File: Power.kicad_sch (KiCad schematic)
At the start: 0 parts

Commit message: Updated power and MCU schem
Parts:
- added C10: 1uF, PCM_JLCPCB:C_0603, symbol PCM_JLCPCB-Capacitors:0603,1uF
- added C11: 2.2uF, PCM_JLCPCB:C_0603, symbol PCM_JLCPCB-Capacitors:0603,2.2uF
- added J1: Conn_01x02, symbol Connector_Generic:Conn_01x02
- added SW1: SW_Push, symbol Switch:SW_Push
- added U6: NPM1300-QEAA-R7, QFN32_5X5_NOR, symbol 2026-04-08_23-52-45:NPM1300-QEAA-R7
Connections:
- new net +BATT: C11.1, U6.19 (VBAT)
- new net GND: C10.2, C11.2, SW1.1, U6.18 (NTC)
- new net NPM_INT: U6.8 (GPIO1)
- new net RESET: SW1.2, U6.7 (GPIO0)
- new net VBUS: C10.1, U6.21 (VBUS)

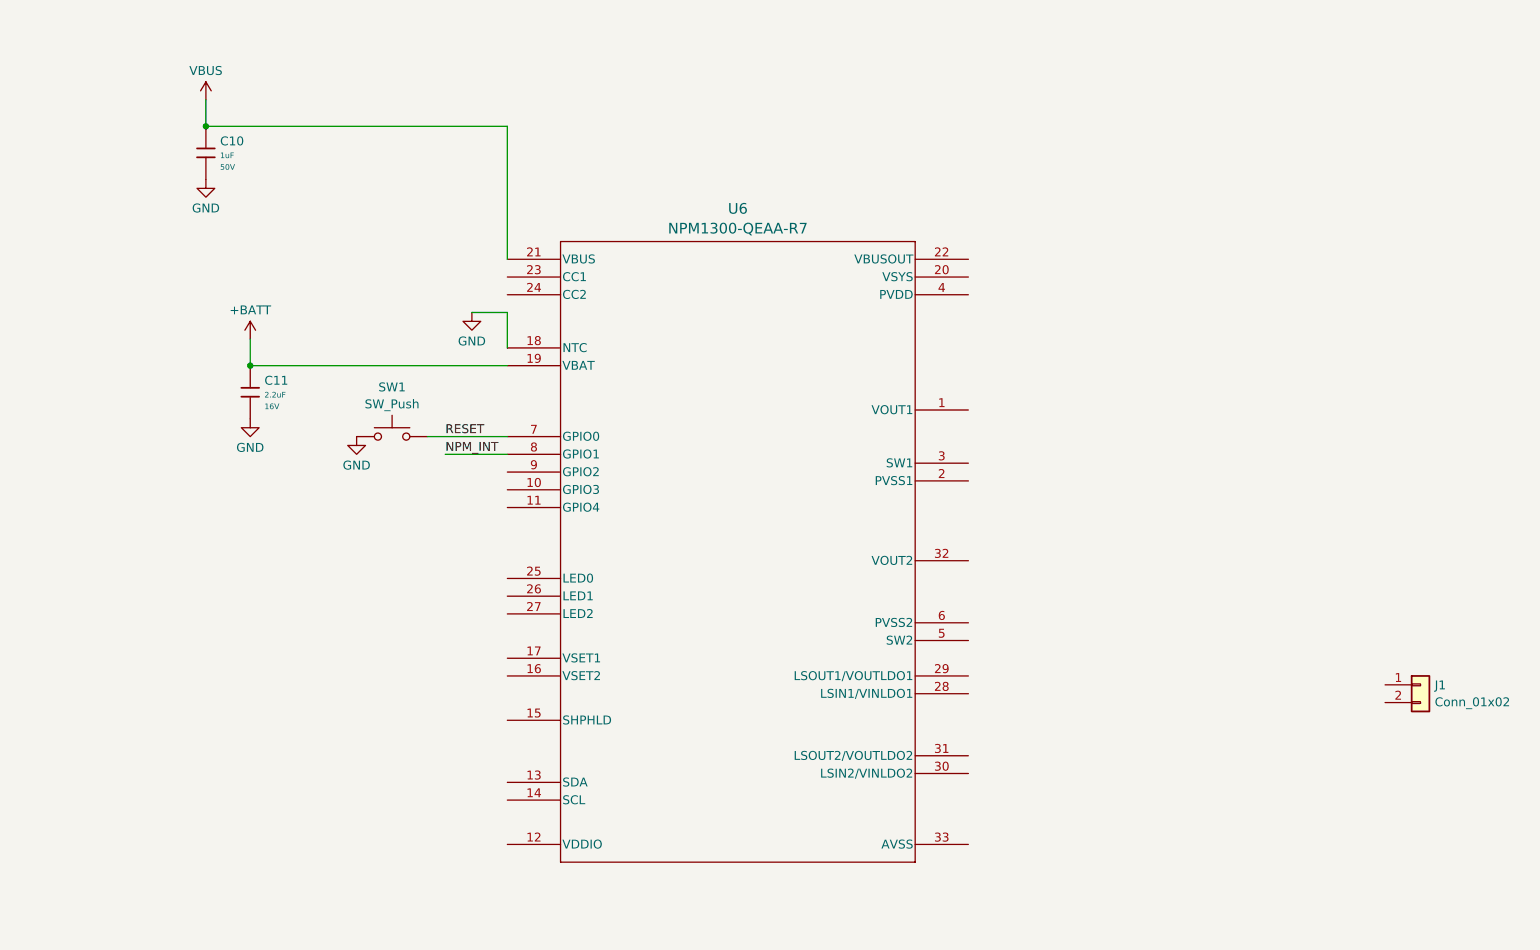
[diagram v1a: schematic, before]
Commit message: PMIC integration
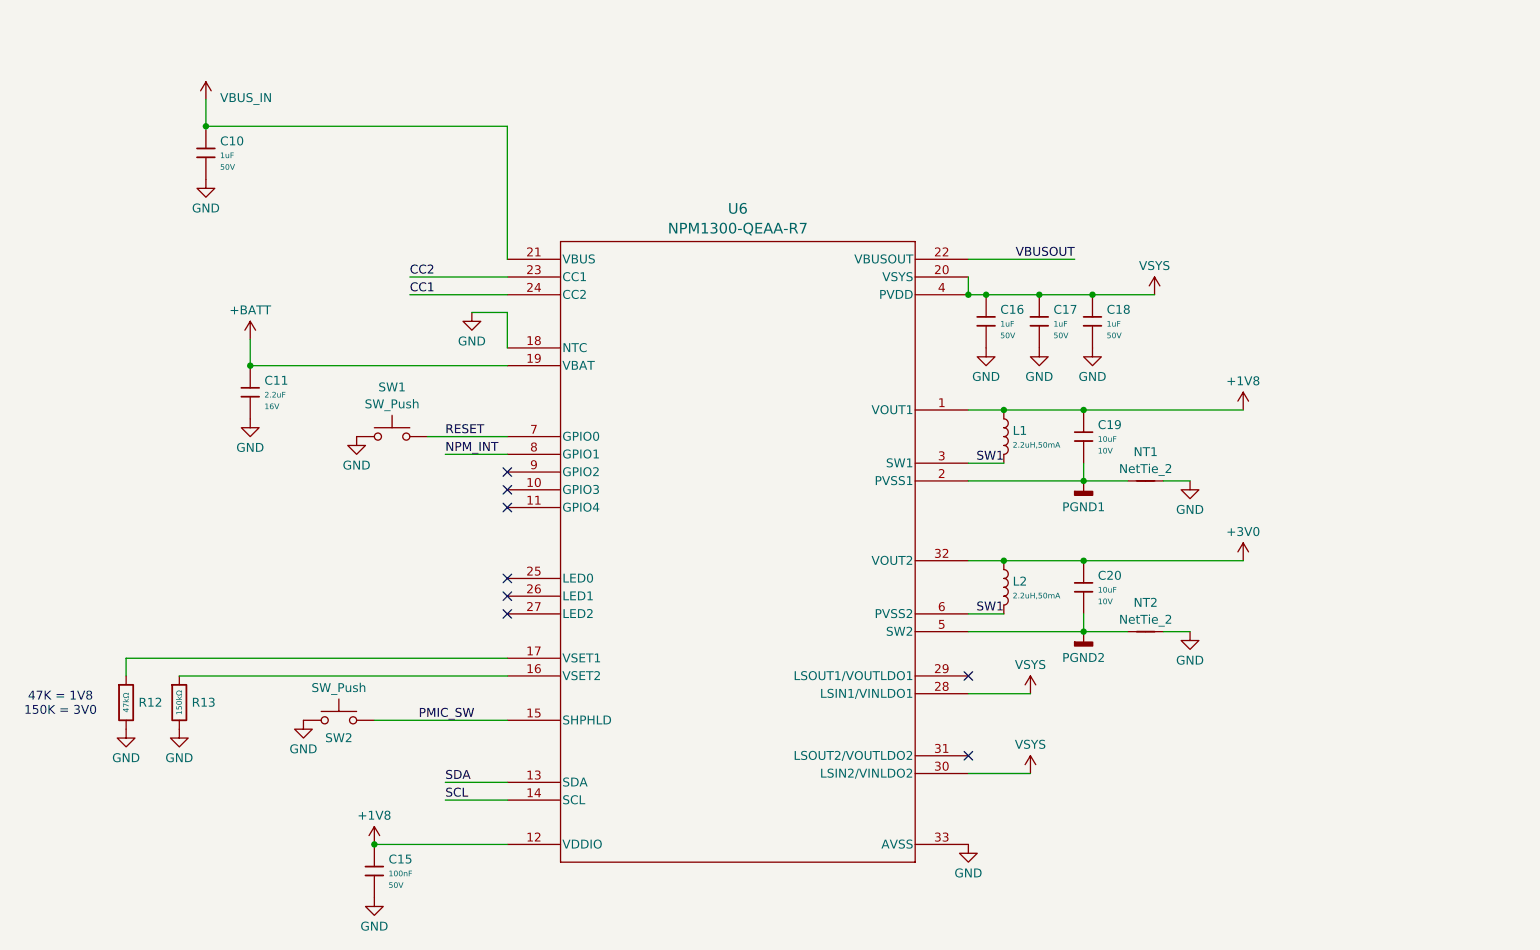
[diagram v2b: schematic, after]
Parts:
- removed J1: Conn_01x02, symbol Connector_Generic:Conn_01x02
- added C15: 100nF, PCM_JLCPCB:C_0603, symbol PCM_JLCPCB-Capacitors:0603,100nF
- added C16, C17, C18: 1uF, PCM_JLCPCB:C_0603, symbol PCM_JLCPCB-Capacitors:0603,1uF
- added C19, C20: 10uF, PCM_JLCPCB:C_0603, symbol PCM_JLCPCB-Capacitors:0603,10uF
- added L1, L2: 2.2uH,50mA, PCM_JLCPCB:L_0805, symbol PCM_JLCPCB-Inductors:2.2uH,50mA
- added NT1, NT2: NetTie_2, symbol Device:NetTie_2
- added R12: 47kΩ, PCM_JLCPCB:R_0603, symbol PCM_JLCPCB-Resistors:0603,47kΩ
- added R13: 150kΩ, PCM_JLCPCB:R_0603, symbol PCM_JLCPCB-Resistors:0603,150kΩ
- added SW2: SW_Push, symbol Switch:SW_Push
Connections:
- net GND: now also U6.33 (AVSS), C15.2, C16.2, C17.2, C18.2, NT1.2, NT2.2, R12.2, R13.2, SW2.1
- net +1V8: now reaches U6.1 (VOUT1)
- net +1V8: now also U6.12 (VDDIO), C15.1, C19.1, L1.1
- net SDA: now reaches U6.13 (SDA)
- net SCL: now reaches U6.14 (SCL)
- net PMIC_SW: now reaches U6.15 (SHPHLD)
- net PMIC_SW: now also SW2.2
- net at U6.16 (VSET2): now also R13.1
- net at U6.17 (VSET1): now also R12.1
- net PGND1: now reaches U6.2 (PVSS1)
- net PGND1: now also C19.2, NT1.1
- net VSYS: now reaches U6.20 (VSYS)
- net VSYS: now also U6.28 (LSIN1/VINLDO1), U6.30 (LSIN2/VINLDO2), U6.4 (PVDD), C16.1, C17.1, C18.1
- net VBUSOUT: now reaches U6.22 (VBUSOUT)
- net CC2: now reaches U6.23 (CC1)
- net CC1: now reaches U6.24 (CC2)
- net SW1: now reaches U6.3 (SW1)
- net SW1: now also U6.6 (PVSS2), L1.2, L2.2
- net +3V0: now reaches U6.32 (VOUT2)
- net +3V0: now also C20.1, L2.1
- net PGND2: now reaches U6.5 (SW2)
- net PGND2: now also C20.2, NT2.1
- net VBUS renamed VBUS_IN
- no-connect marks 0 -> 8
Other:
- note added: "47K = 1V8 150K = 3V0"

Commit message: Updated MCU
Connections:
- net VBUSOUT renamed VBUS_OUT
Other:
- note added: "PMIC"
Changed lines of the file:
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@@
+		)
+	)
+	(text "PMIC"
+		(exclude_from_sim no)
+		(at 132.588 44.45 0)
+		(effects
+			(font
+				(size 3 3)
+				(thickness 0.6)
+				(bold yes)
+			)
 		)
 	)
@@
 		)
 	)
-	(label "VBUSOUT"
+	(label "VBUS_OUT"
 		(at 182.88 58.42 180)
 		(effects

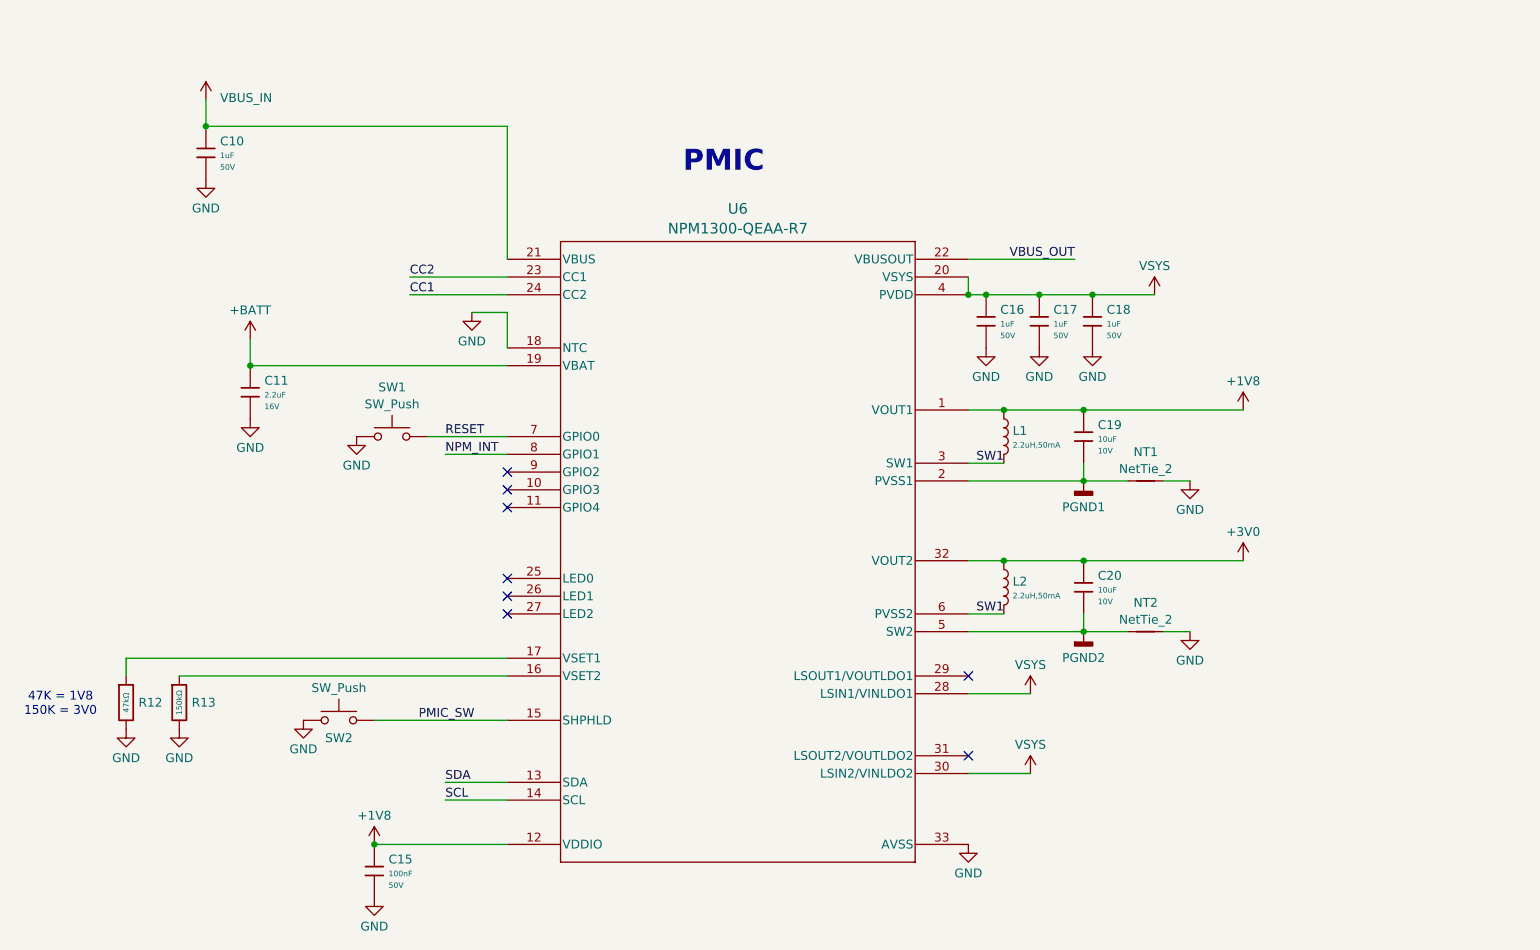
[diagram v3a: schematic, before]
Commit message: Fixed Hierarchical Labels
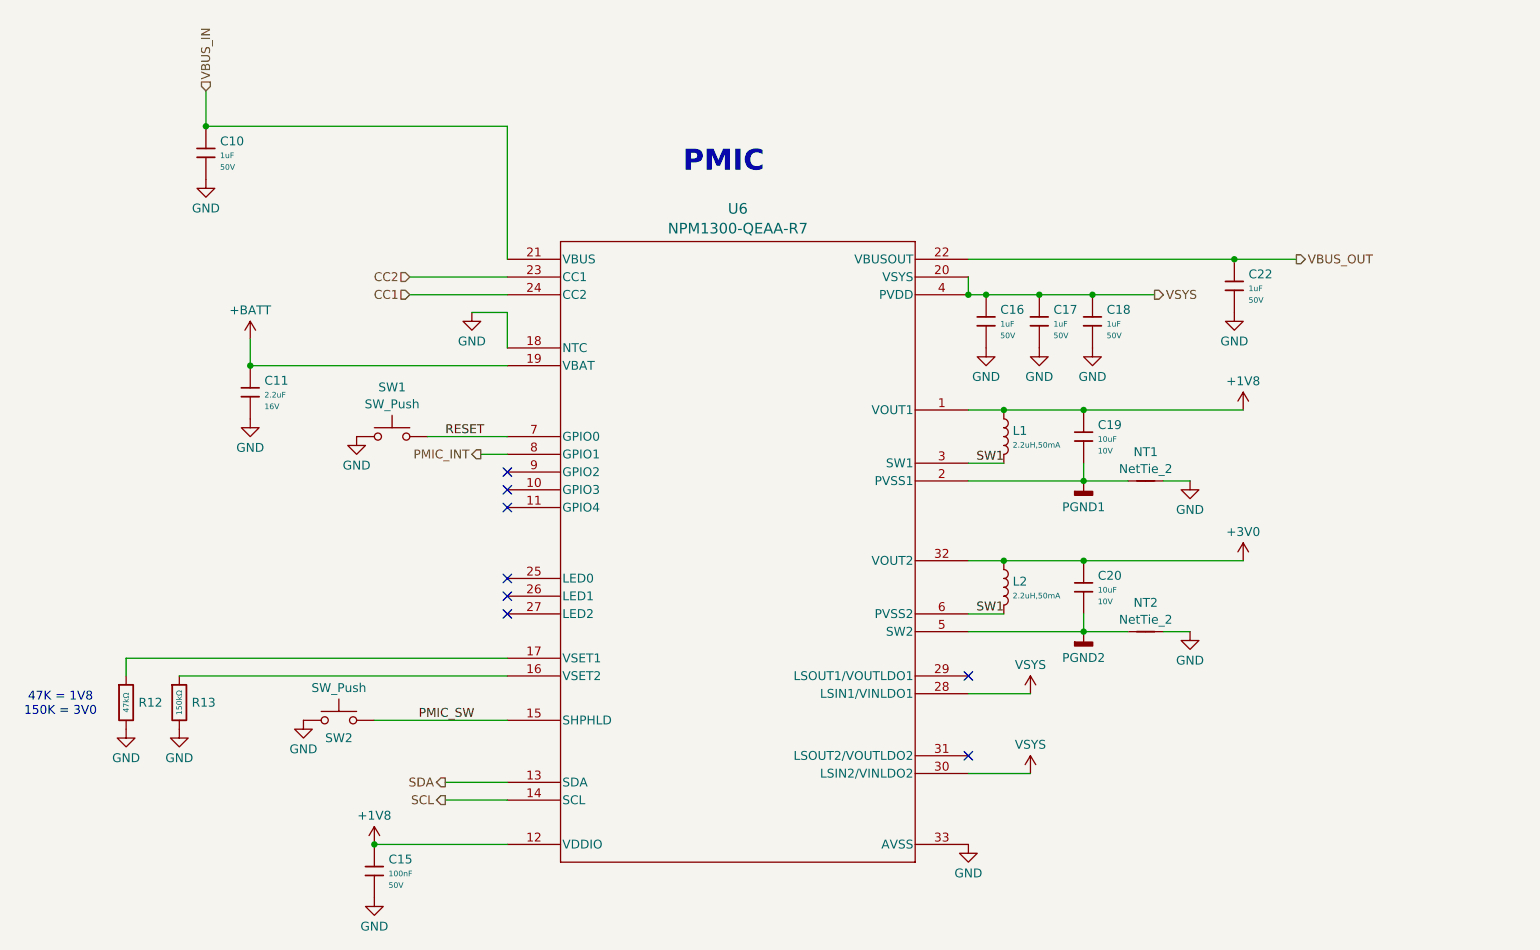
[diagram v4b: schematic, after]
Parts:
- added C22: 1uF, PCM_JLCPCB:C_0603, symbol PCM_JLCPCB-Capacitors:0603,1uF
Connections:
- net GND: now also C22.2
- net VBUS_OUT: now also C22.1
- net NPM_INT renamed PMIC_INT

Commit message: Added clock and updated schem
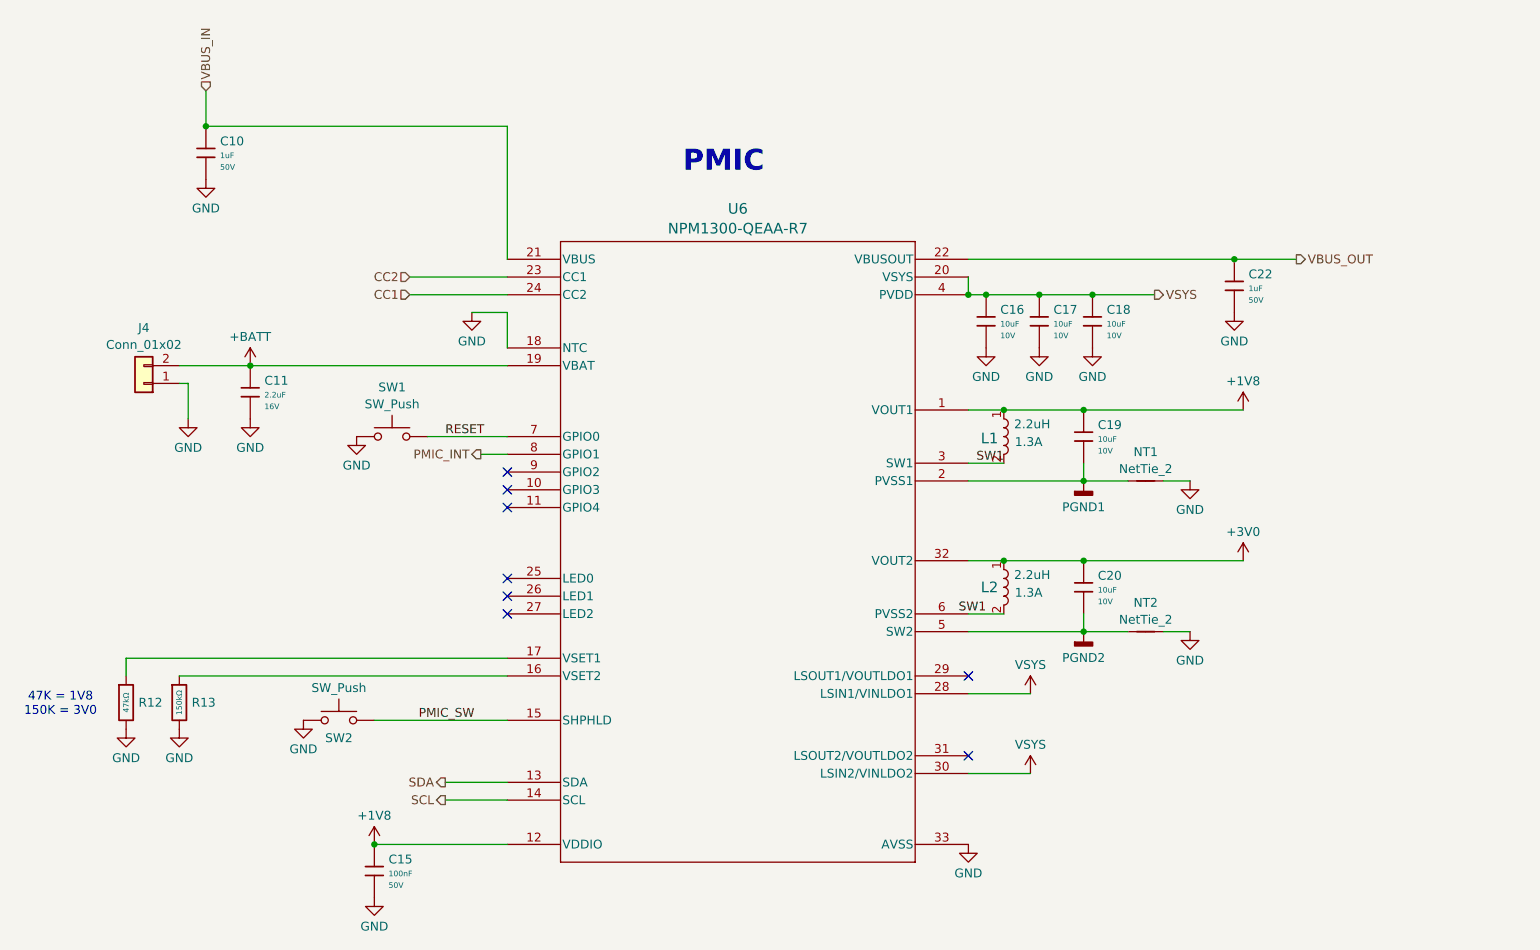
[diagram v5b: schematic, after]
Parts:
- removed C16, C17, C18: 1uF, PCM_JLCPCB:C_0603, symbol PCM_JLCPCB-Capacitors:0603,1uF
- removed L1, L2: 2.2uH,50mA, PCM_JLCPCB:L_0805, symbol PCM_JLCPCB-Inductors:2.2uH,50mA
- added C16, C17, C18: 10uF, PCM_JLCPCB:C_0603, symbol PCM_JLCPCB-Capacitors:0603,10uF
- added J4: Conn_01x02, symbol Connector_Generic:Conn_01x02
- added L1, L2: LQM2HPN2R2MG0L, IND_LQM2HPN2R2MG0L_MUR, symbol 2026-04-16_01-05-19:LQM2HPN2R2MG0L
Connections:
- net +1V8: now also L1.1
- net +3V0: now also L2.1
- net +BATT: now also J4.2 (Pin_2)
- net GND: now also C16.2, C17.2, C18.2, J4.1 (Pin_1)
- net SW1: now also L1.2, L2.2
- net VSYS: now also C16.1, C17.1, C18.1

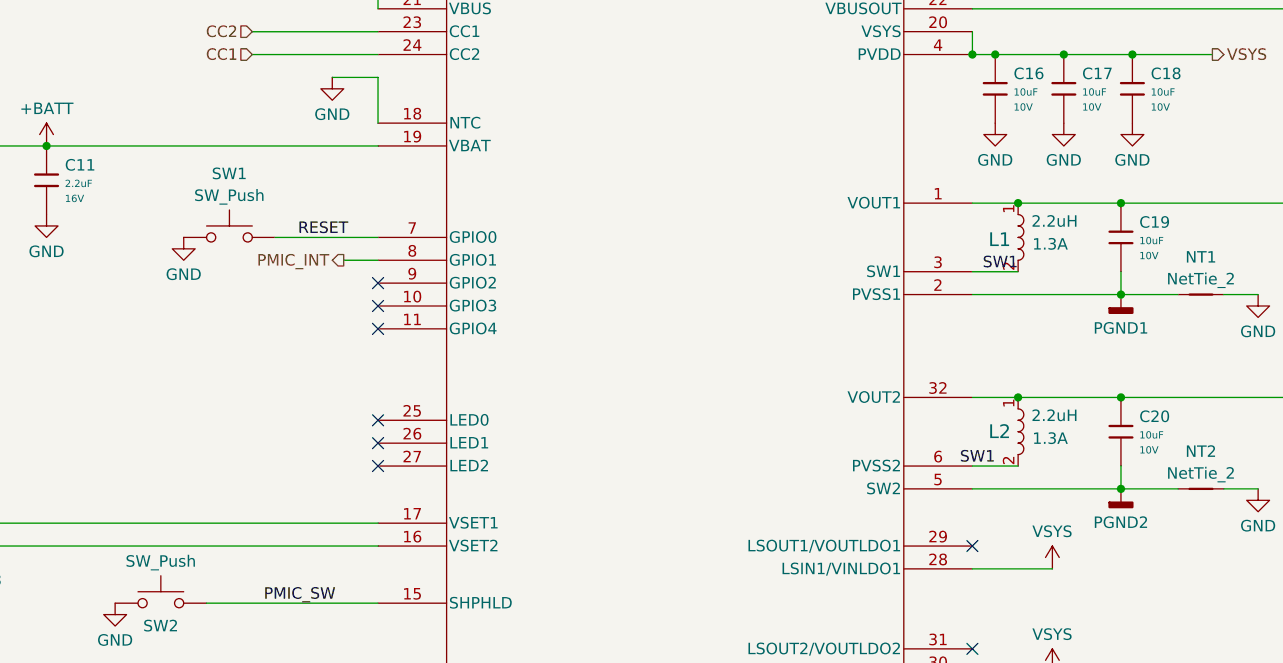
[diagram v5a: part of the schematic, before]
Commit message: Updated Schem and Organized Layout
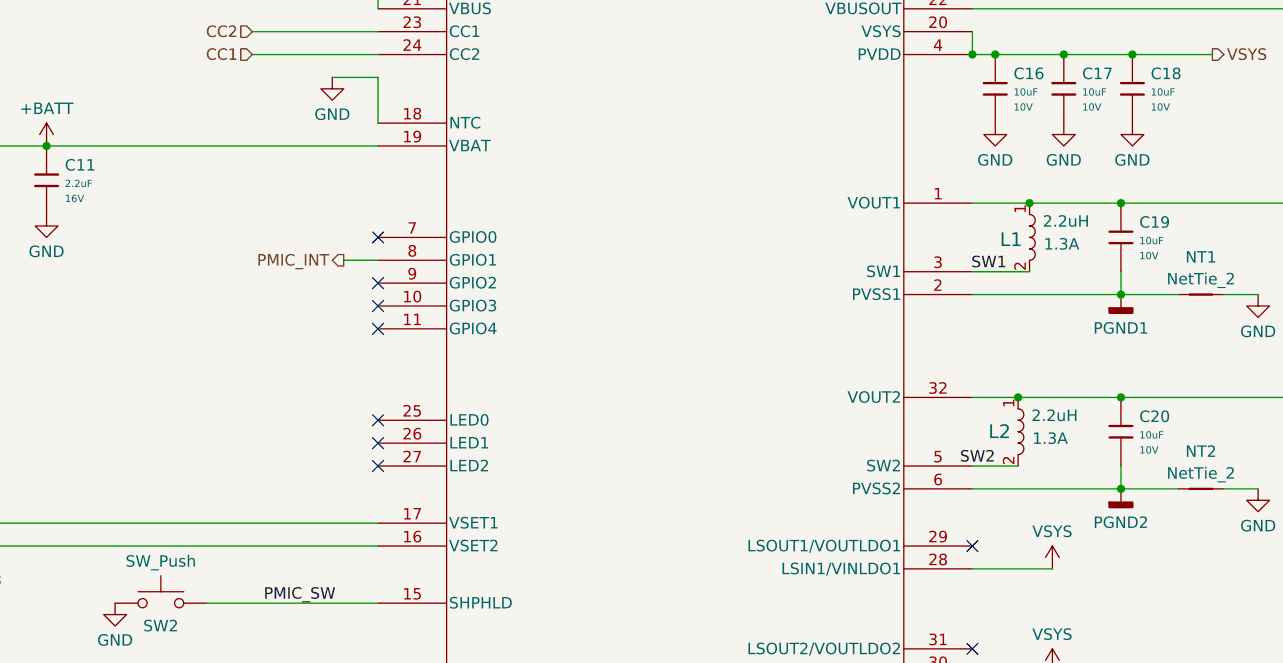
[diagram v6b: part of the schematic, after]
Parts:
- removed SW1: SW_Push, symbol Switch:SW_Push
- C10, C11, C16, C17, C18, C19, C20, C22: Manufacturer Samsung Electro-Mechanics -> (none)
- C15: Manufacturer YAGEO -> (none)
- J4: footprint (none) -> Connector_JST:JST_PH_S2B-PH-K_1x02_P2.00mm_Horizontal
- L1, L2: footprint IND_LQM2HPN2R2MG0L_MUR -> LQM:IND_LQM2HPN2R2MG0L_MUR
- NT1, NT2: footprint (none) -> NetTie:NetTie-2_SMD_Pad0.5mm
- R12, R13: Manufacturer UNI-ROYAL(Uniroyal Elec) -> (none)
- SW2: footprint (none) -> SKRPACE:SW_SKRPACE010_AAL
- U6: footprint QFN32_5X5_NOR -> NPM:QFN32_5X5_NOR
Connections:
- net PGND2: now also U6.6 (PVSS2); no longer U6.5 (SW2)
- net SW1: no longer L2.2, U6.6 (PVSS2)
- net RESET: no longer names the net of U6.7 (GPIO0)
- new net SW2: L2.2, U6.5 (SW2)
- no-connect marks 8 -> 9
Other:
- moved on the sheet: L1
